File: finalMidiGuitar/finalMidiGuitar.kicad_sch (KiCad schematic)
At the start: 11 parts, among them J1 NeoPixel, J3 NeoPixel, J4 Oled Display, M1 Module_XIAO_Generic_SocketSMD, SW1 BTN, U1 SN74LVC1T45DBVR

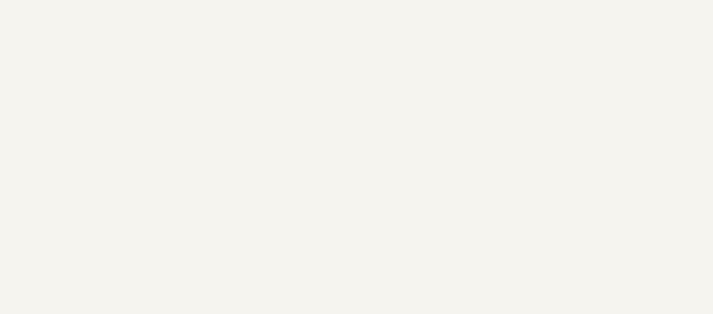
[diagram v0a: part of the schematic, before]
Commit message: Add label "Midi Guitar" to the schematic for better identification
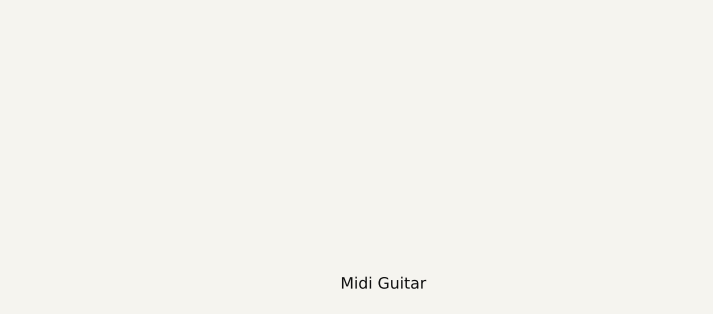
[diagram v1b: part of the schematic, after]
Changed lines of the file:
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@@
+		)
+	)
+	(label "Midi Guitar"
+		(at 186.69 190.5 0)
+		(effects
+			(font
+				(size 1.27 1.27)
+			)
+			(justify left bottom)
 		)
 	)
